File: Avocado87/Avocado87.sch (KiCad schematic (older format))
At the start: 185 parts, among them U1 proton_c

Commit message: Add footprint for proton-c
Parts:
- U1: footprint (none) -> proton_c:proton_c
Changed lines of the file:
@@
 F 0 "U1" H 9825 1027 50  0000 C CNN
 F 1 "proton_c" H 9825 936 50  0000 C CNN
-F 2 "" H 9700 2550 50  0001 C CNN
+F 2 "proton_c:proton_c" H 9700 2550 50  0001 C CNN
 F 3 "" H 9700 2550 50  0001 C CNN
 	1    9850 2550

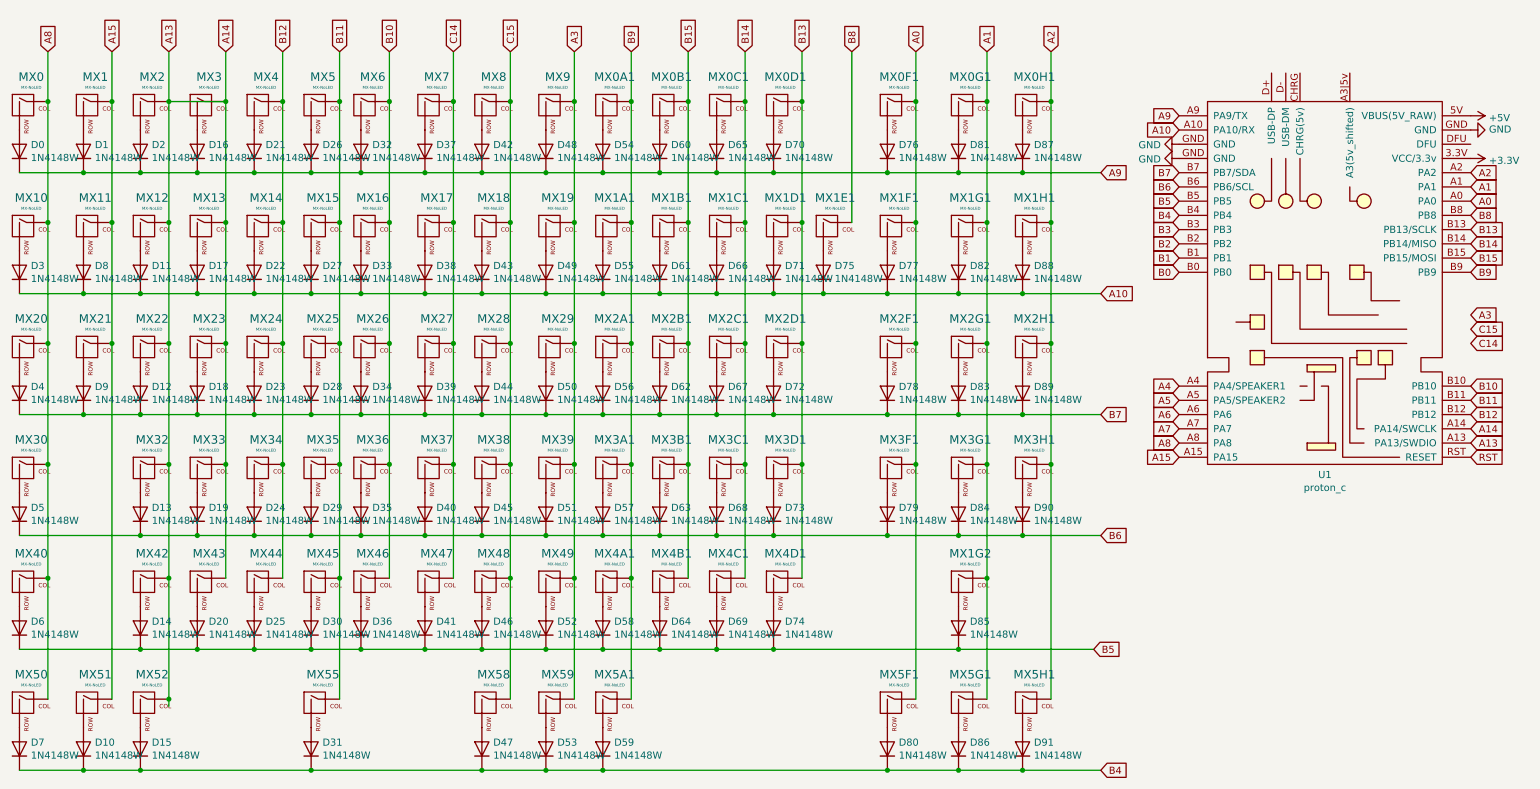
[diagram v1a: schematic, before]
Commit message: Footprint work
 - sort out issues with naming and missing switches
 - remove unused symbols from proton-c
 - start labeling diodes correctly
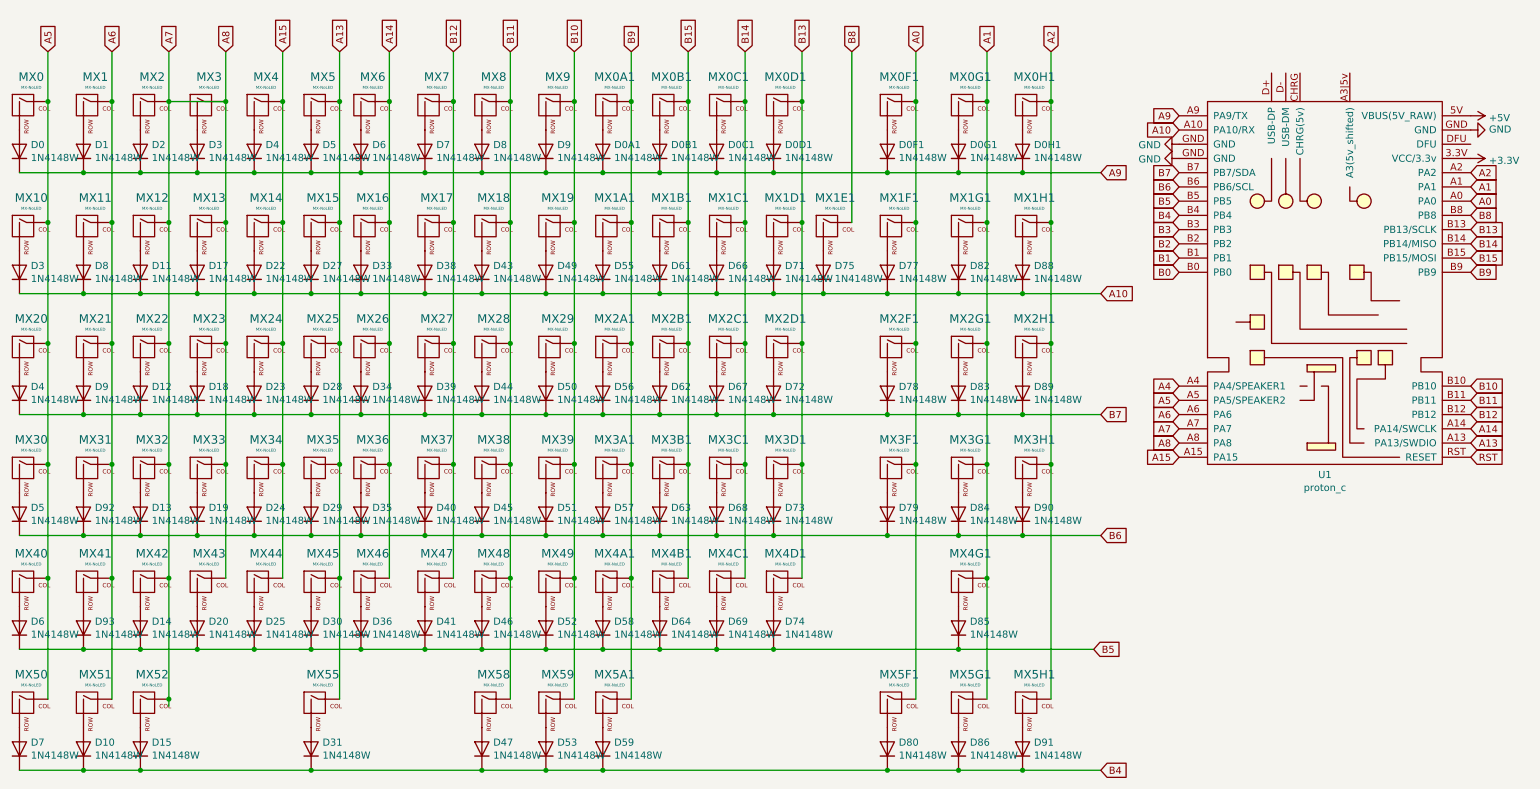
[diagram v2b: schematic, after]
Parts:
- added D92, D93: 1N4148W, Diodes_SMD:D_SOD-123, symbol Diode:1N4148W
- added MX31, MX41: MX-NoLED, MX_Only:MXOnly-1U-NoLED, symbol MX_Alps_Hybrid:MX-NoLED
- D0, D1, D10, D11, D12, D13, D14, D15, D17, D18, D19, D2, D20, D22, D23, D24, D25, D27, D28, D29, D3, D30, D31, D33, D34, D35, D36, D38, D39, D4, D40, D41, D43, D44, D45, D46, D47, D49, D5, D50, D51, D52, D53, D55, D56, D57, D58, D59, D6, D61, D62, D63, D64, D66, D67, D68, D69, D7, D71, D72, D73, D74, D75, D77, D78, D79, D8, D80, D82, D83, D84, D85, D86, D88, D89, D9, D90, D91: footprint Diode_SMD:D_SOD-123 -> Diodes_SMD:D_SOD-123
- D0A1: renamed from D54; footprint Diode_SMD:D_SOD-123 -> Diodes_SMD:D_SOD-123
- D0B1: renamed from D60; footprint Diode_SMD:D_SOD-123 -> Diodes_SMD:D_SOD-123
- D0C1: renamed from D65; footprint Diode_SMD:D_SOD-123 -> Diodes_SMD:D_SOD-123
- D0D1: renamed from D70; footprint Diode_SMD:D_SOD-123 -> Diodes_SMD:D_SOD-123
- D0F1: renamed from D76; footprint Diode_SMD:D_SOD-123 -> Diodes_SMD:D_SOD-123
- D0G1: renamed from D81; footprint Diode_SMD:D_SOD-123 -> Diodes_SMD:D_SOD-123
- D0H1: renamed from D87; footprint Diode_SMD:D_SOD-123 -> Diodes_SMD:D_SOD-123
- D3: renamed from D16; footprint Diode_SMD:D_SOD-123 -> Diodes_SMD:D_SOD-123
- D4: renamed from D21; footprint Diode_SMD:D_SOD-123 -> Diodes_SMD:D_SOD-123
- D5: renamed from D26; footprint Diode_SMD:D_SOD-123 -> Diodes_SMD:D_SOD-123
- D6: renamed from D32; footprint Diode_SMD:D_SOD-123 -> Diodes_SMD:D_SOD-123
- D7: renamed from D37; footprint Diode_SMD:D_SOD-123 -> Diodes_SMD:D_SOD-123
- D8: renamed from D42; footprint Diode_SMD:D_SOD-123 -> Diodes_SMD:D_SOD-123
- D9: renamed from D48; footprint Diode_SMD:D_SOD-123 -> Diodes_SMD:D_SOD-123
- renumbered MX1G2 to MX4G1
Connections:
- net A3 is gone; now on net B10: MX19.1 (COL), MX29.1 (COL), MX39.1 (COL), MX49.1 (COL), MX59.1 (COL), MX9.1 (COL)
- net C14 is gone; now on net B12: MX17.1 (COL), MX27.1 (COL), MX37.1 (COL), MX47.1 (COL), MX7.1 (COL)
- net C15 is gone; now on net B11: MX18.1 (COL), MX28.1 (COL), MX38.1 (COL), MX48.1 (COL), MX58.1 (COL), MX8.1 (COL)
- net A13: now also MX15.1 (COL), MX25.1 (COL), MX35.1 (COL), MX45.1 (COL), MX5.1 (COL), MX55.1 (COL); no longer MX12.1 (COL), MX13.1 (COL), MX2.1 (COL), MX22.1 (COL), MX23.1 (COL), MX3.1 (COL), MX32.1 (COL), MX33.1 (COL), MX42.1 (COL), MX43.1 (COL), MX52.1 (COL), U1.A14 (PA14/SWCLK)
- net A15: now also MX14.1 (COL), MX24.1 (COL), MX34.1 (COL), MX4.1 (COL), MX44.1 (COL); no longer MX1.1 (COL), MX11.1 (COL), MX21.1 (COL), MX51.1 (COL)
- net A5: now also MX0.1 (COL), MX10.1 (COL), MX20.1 (COL), MX30.1 (COL), MX40.1 (COL), MX50.1 (COL)
- net A6: now also MX1.1 (COL), MX11.1 (COL), MX21.1 (COL), MX51.1 (COL), MX31.1 (COL), MX41.1 (COL)
- net A7: now also MX12.1 (COL), MX13.1 (COL), MX2.1 (COL), MX22.1 (COL), MX23.1 (COL), MX3.1 (COL), MX32.1 (COL), MX33.1 (COL), MX42.1 (COL), MX43.1 (COL), MX52.1 (COL), U1.A8 (PA8)
- net B10: no longer MX16.1 (COL), MX26.1 (COL), MX36.1 (COL), MX46.1 (COL), MX6.1 (COL)
- net B11: no longer MX15.1 (COL), MX25.1 (COL), MX35.1 (COL), MX45.1 (COL), MX5.1 (COL), MX55.1 (COL)
- net B12: no longer MX14.1 (COL), MX24.1 (COL), MX34.1 (COL), MX4.1 (COL), MX44.1 (COL)
- net B5: now also D93.1 (K)
- net B6: now also D92.1 (K)
- removed net A8: MX0.1 (COL), MX10.1 (COL), MX20.1 (COL), MX30.1 (COL), MX40.1 (COL), MX50.1 (COL), U1.A8 (PA8)
- new net: D92.2 (A), MX31.2 (ROW)
- new net: D93.2 (A), MX41.2 (ROW)
- new net A14: MX16.1 (COL), MX26.1 (COL), MX36.1 (COL), MX46.1 (COL), MX6.1 (COL), U1.A14 (PA14/SWCLK)

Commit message: Placement and renames
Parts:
- removed D73, D74: 1N4148W, Diodes_SMD:D_SOD-123, symbol Diode:1N4148W
- removed MX3D1, MX4D1: MX-NoLED, MX_Only:MXOnly-1U-NoLED, symbol MX_Alps_Hybrid:MX-NoLED
- renumbered D3 to D10, D8 to D11, D11 to D12, D17 to D13, D22 to D14, D27 to D15, D33 to D16, D38 to D17, D43 to D18, D49 to D19, D55 to D1A1, D61 to D1B1, D66 to D1C1, D71 to D1D1, D75 to D1E1, D77 to D1F1, D82 to D1G1, D88 to D1H1, D4 to D20, D9 to D21, D12 to D22, D18 to D23, D23 to D24, D28 to D25, D34 to D26, D39 to D27, D44 to D28, D50 to D29, D56 to D2A1, D62 to D2B1, D67 to D2C1, D72 to D2D1, D78 to D2F1, D83 to D2G1, D89 to D2H1, D5 to D30, D92 to D31, D13 to D32, D19 to D33, D24 to D34, D29 to D35, D35 to D36, D40 to D37, D45 to D38, D51 to D39, D57 to D3A1, D63 to D3B1, D68 to D3C1, D79 to D3F1, D84 to D3G1, D90 to D3H1, D6 to D40, D93 to D41, D14 to D42, D20 to D43, D25 to D44, D30 to D45, D36 to D46, D41 to D47, D46 to D48, D52 to D49, D58 to D4A1, D64 to D4B1, D69 to D4C1, D85 to D4G1, D7 to D50, D10 to D51, D15 to D52, D31 to D53, D47 to D58, D53 to D59, D59 to D5A1, D80 to D5F1, D86 to D5G1, D91 to D5H1

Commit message: Routed PCB
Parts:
- renumbered D53 to D55
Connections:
- net A0: now also MX0C1.1 (COL), MX1C1.1 (COL), MX2C1.1 (COL), MX3C1.1 (COL), MX4C1.1 (COL); no longer MX0F1.1 (COL), MX1F1.1 (COL), MX2F1.1 (COL), MX3F1.1 (COL), MX5F1.1 (COL)
- net A1: now also MX0D1.1 (COL), MX1D1.1 (COL), MX2D1.1 (COL); no longer MX0G1.1 (COL), MX1G1.1 (COL), MX2G1.1 (COL), MX3G1.1 (COL), MX4G1.1 (COL), MX5G1.1 (COL)
- net A10: now also MX0F1.1 (COL), MX1F1.1 (COL), MX2F1.1 (COL), MX3F1.1 (COL), MX5F1.1 (COL); no longer D10.1 (K), D11.1 (K), D12.1 (K), D13.1 (K), D14.1 (K), D15.1 (K), D16.1 (K), D17.1 (K), D18.1 (K), D19.1 (K), D1A1.1 (K), D1B1.1 (K), D1C1.1 (K), D1D1.1 (K), D1E1.1 (K), D1F1.1 (K), D1G1.1 (K), D1H1.1 (K)
- net A13: now also MX17.1 (COL), MX27.1 (COL), MX37.1 (COL), MX47.1 (COL), MX7.1 (COL); no longer MX15.1 (COL), MX25.1 (COL), MX35.1 (COL), MX45.1 (COL), MX5.1 (COL), MX55.1 (COL)
- net A15: now also D30.1 (K), D31.1 (K), D32.1 (K), D33.1 (K), D34.1 (K), D35.1 (K), D36.1 (K), D37.1 (K), D38.1 (K), D39.1 (K), D3A1.1 (K), D3B1.1 (K), D3C1.1 (K), D3F1.1 (K), D3G1.1 (K), D3H1.1 (K); no longer MX14.1 (COL), MX24.1 (COL), MX34.1 (COL), MX4.1 (COL), MX44.1 (COL)
- net A2: now also D0.1 (K), D0A1.1 (K), D0B1.1 (K), D0C1.1 (K), D0D1.1 (K), D0F1.1 (K), D0G1.1 (K), D0H1.1 (K), D1.1 (K), D2.1 (K), D3.1 (K), D4.1 (K), D5.1 (K), D6.1 (K), D7.1 (K), D8.1 (K), D9.1 (K); no longer MX0H1.1 (COL), MX1H1.1 (COL), MX2H1.1 (COL), MX3H1.1 (COL), MX5H1.1 (COL)
- net A5: no longer MX0.1 (COL), MX10.1 (COL), MX20.1 (COL), MX30.1 (COL), MX40.1 (COL), MX50.1 (COL)
- net A6: no longer MX1.1 (COL), MX11.1 (COL), MX21.1 (COL), MX31.1 (COL), MX41.1 (COL), MX51.1 (COL)
- net A7: now also D50.1 (K), D51.1 (K), D52.1 (K), D55.1 (K), D58.1 (K), D59.1 (K), D5A1.1 (K), D5F1.1 (K), D5G1.1 (K), D5H1.1 (K); no longer MX12.1 (COL), MX13.1 (COL), MX2.1 (COL), MX22.1 (COL), MX23.1 (COL), MX3.1 (COL), MX32.1 (COL), MX33.1 (COL), MX42.1 (COL), MX43.1 (COL), MX52.1 (COL), U1.A8 (PA8)
- net A9: now also MX0G1.1 (COL), MX1G1.1 (COL), MX2G1.1 (COL), MX3G1.1 (COL), MX4G1.1 (COL), MX5G1.1 (COL); no longer D0.1 (K), D0A1.1 (K), D0B1.1 (K), D0C1.1 (K), D0D1.1 (K), D0F1.1 (K), D0G1.1 (K), D0H1.1 (K), D1.1 (K), D2.1 (K), D3.1 (K), D4.1 (K), D5.1 (K), D6.1 (K), D7.1 (K), D8.1 (K), D9.1 (K)
- net B1: now also MX0B1.1 (COL), MX1B1.1 (COL), MX2B1.1 (COL), MX3B1.1 (COL), MX4B1.1 (COL)
- net B10: now also MX13.1 (COL), MX23.1 (COL), MX3.1 (COL), MX33.1 (COL), MX43.1 (COL); no longer MX19.1 (COL), MX29.1 (COL), MX39.1 (COL), MX49.1 (COL), MX59.1 (COL), MX9.1 (COL)
- net B11: now also MX14.1 (COL), MX24.1 (COL), MX34.1 (COL), MX4.1 (COL), MX44.1 (COL); no longer MX18.1 (COL), MX28.1 (COL), MX38.1 (COL), MX48.1 (COL), MX58.1 (COL), MX8.1 (COL)
- net B12: now also MX15.1 (COL), MX25.1 (COL), MX35.1 (COL), MX45.1 (COL), MX5.1 (COL), MX55.1 (COL); no longer MX17.1 (COL), MX27.1 (COL), MX37.1 (COL), MX47.1 (COL), MX7.1 (COL)
- net B13: now also MX0.1 (COL), MX10.1 (COL), MX20.1 (COL), MX30.1 (COL), MX40.1 (COL), MX50.1 (COL); no longer MX0D1.1 (COL), MX1D1.1 (COL), MX2D1.1 (COL)
- net B14: now also MX1.1 (COL), MX11.1 (COL), MX21.1 (COL), MX31.1 (COL), MX41.1 (COL), MX51.1 (COL); no longer MX0C1.1 (COL), MX1C1.1 (COL), MX2C1.1 (COL), MX3C1.1 (COL), MX4C1.1 (COL)
- net B15: now also MX12.1 (COL), MX2.1 (COL), MX22.1 (COL), MX32.1 (COL), MX42.1 (COL), MX52.1 (COL); no longer MX0B1.1 (COL), MX1B1.1 (COL), MX2B1.1 (COL), MX3B1.1 (COL), MX4B1.1 (COL)
- net B2: now also MX0A1.1 (COL), MX1A1.1 (COL), MX2A1.1 (COL), MX3A1.1 (COL), MX4A1.1 (COL), MX5A1.1 (COL)
- net B3: now also MX19.1 (COL), MX29.1 (COL), MX39.1 (COL), MX49.1 (COL), MX59.1 (COL), MX9.1 (COL)
- net B4: now also MX18.1 (COL), MX28.1 (COL), MX38.1 (COL), MX48.1 (COL), MX58.1 (COL), MX8.1 (COL); no longer D50.1 (K), D51.1 (K), D52.1 (K), D55.1 (K), D58.1 (K), D59.1 (K), D5A1.1 (K), D5F1.1 (K), D5G1.1 (K), D5H1.1 (K)
- net B5: no longer D40.1 (K), D41.1 (K), D42.1 (K), D43.1 (K), D44.1 (K), D45.1 (K), D46.1 (K), D47.1 (K), D48.1 (K), D49.1 (K), D4A1.1 (K), D4B1.1 (K), D4C1.1 (K), D4G1.1 (K)
- net B6: now also D10.1 (K), D11.1 (K), D12.1 (K), D13.1 (K), D14.1 (K), D15.1 (K), D16.1 (K), D17.1 (K), D18.1 (K), D19.1 (K), D1A1.1 (K), D1B1.1 (K), D1C1.1 (K), D1D1.1 (K), D1E1.1 (K), D1F1.1 (K), D1G1.1 (K), D1H1.1 (K); no longer D30.1 (K), D31.1 (K), D32.1 (K), D33.1 (K), D34.1 (K), D35.1 (K), D36.1 (K), D37.1 (K), D38.1 (K), D39.1 (K), D3A1.1 (K), D3B1.1 (K), D3C1.1 (K), D3F1.1 (K), D3G1.1 (K), D3H1.1 (K)
- net B7: now also MX0H1.1 (COL), MX1H1.1 (COL), MX2H1.1 (COL), MX3H1.1 (COL), MX5H1.1 (COL); no longer D20.1 (K), D21.1 (K), D22.1 (K), D23.1 (K), D24.1 (K), D25.1 (K), D26.1 (K), D27.1 (K), D28.1 (K), D29.1 (K), D2A1.1 (K), D2B1.1 (K), D2C1.1 (K), D2D1.1 (K), D2F1.1 (K), D2G1.1 (K), D2H1.1 (K)
- net B9: now also D20.1 (K), D21.1 (K), D22.1 (K), D23.1 (K), D24.1 (K), D25.1 (K), D26.1 (K), D27.1 (K), D28.1 (K), D29.1 (K), D2A1.1 (K), D2B1.1 (K), D2C1.1 (K), D2D1.1 (K), D2F1.1 (K), D2G1.1 (K), D2H1.1 (K); no longer MX0A1.1 (COL), MX1A1.1 (COL), MX2A1.1 (COL), MX3A1.1 (COL), MX4A1.1 (COL), MX5A1.1 (COL)
- new net A8: D40.1 (K), D41.1 (K), D42.1 (K), D43.1 (K), D44.1 (K), D45.1 (K), D46.1 (K), D47.1 (K), D48.1 (K), D49.1 (K), D4A1.1 (K), D4B1.1 (K), D4C1.1 (K), D4G1.1 (K), U1.A8 (PA8)
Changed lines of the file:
@@
 $EndComp
 $Comp
-L Diode:1N4148W D53
+L Diode:1N4148W D55
 U 1 1 5DA675DF
 P 2700 6000
-F 0 "D53" V 2746 5920 50  0000 R CNN
+F 0 "D55" V 2746 5920 50  0000 R CNN
 F 1 "1N4148W" V 2655 5920 50  0000 R CNN
 F 2 "Diodes_SMD:D_SOD-123" H 2700 5825 50  0001 C CNN
@@
 	1700 4000 1700 4800
 Connection ~ 1700 4000
-Wire Wire Line
-	1700 1450 2100 1450
 Connection ~ 1700 4800
 Wire Wire Line
@@
 Wire Wire Line
 	7700 6150 7250 6150
-Text GLabel 8250 1950 2    50   Input ~ 0
+Text GLabel 7450 1100 1    50   Input ~ 0
 A9
+Text GLabel 7900 1100 1    50   Input ~ 0
+B7
+Text GLabel 6950 1100 1    50   Input ~ 0
+A10
+Text GLabel 8250 2800 2    50   Input ~ 0
+B6
 Text GLabel 8250 3650 2    50   Input ~ 0
-B7
-Text GLabel 8250 2800 2    50   Input ~ 0
-A10
-Text GLabel 8250 4500 2    50   Input ~ 0
-B6
-Text GLabel 8200 5300 2    50   Input ~ 0
-B5
-Text GLabel 8250 6150 2    50   Input ~ 0
-B4
+B9
 Connection ~ 1300 1450
 Wire Wire Line
@@
 Wire Wire Line
 	850  1450 850  1100
-Text GLabel 7900 1100 1    50   Input ~ 0
+Text GLabel 8250 1950 2    50   Input ~ 0
 A2
-Text GLabel 7450 1100 1    50   Input ~ 0
+Text GLabel 6150 1100 1    50   Input ~ 0
 A1
-Text GLabel 6950 1100 1    50   Input ~ 0
+Text GLabel 5750 1100 1    50   Input ~ 0
 A0
 Text GLabel 6500 1100 1    50   Input ~ 0
 B8
-Text GLabel 6150 1100 1    50   Input ~ 0
+Text GLabel 850  1100 1    50   Input ~ 0
 B13
-Text GLabel 5750 1100 1    50   Input ~ 0
+Text GLabel 1300 1100 1    50   Input ~ 0
 B14
-Text GLabel 5350 1100 1    50   Input ~ 0
+Text GLabel 1700 1100 1    50   Input ~ 0
 B15
-Text GLabel 4950 1100 1    50   Input ~ 0
-B9
-Text GLabel 4550 1100 1    50   Input ~ 0
+Text GLabel 8250 4500 2    50   Input ~ 0
+A15
+Text GLabel 2100 1100 1    50   Input ~ 0
 B10
-Text GLabel 4100 1100 1    50   Input ~ 0
+Text GLabel 2500 1100 1    50   Input ~ 0
 B11
-Text GLabel 3700 1100 1    50   Input ~ 0
+Text GLabel 2900 1100 1    50   Input ~ 0
 B12
 Text GLabel 3250 1100 1    50   Input ~ 0
 A14
-Text GLabel 2900 1100 1    50   Input ~ 0
+Text GLabel 3700 1100 1    50   Input ~ 0
 A13
-Text GLabel 2500 1100 1    50   Input ~ 0
-A15
-Text GLabel 2100 1100 1    50   Input ~ 0
+Text GLabel 8200 5300 2    50   Input ~ 0
 A8
-Text GLabel 1700 1100 1    50   Input ~ 0
-A7
-Text GLabel 1300 1100 1    50   Input ~ 0
-A6
-Text GLabel 850  1100 1    50   Input ~ 0
-A5
+Text GLabel 5350 1100 1    50   Input ~ 0
+B1
+Text GLabel 4950 1100 1    50   Input ~ 0
+B2
 $Comp
 L power:+3.3V #PWR0101
@@
 Connection ~ 7250 5300
 Connection ~ 5550 5300
+Text GLabel 4550 1100 1    50   Input ~ 0
+B3
+Text GLabel 4100 1100 1    50   Input ~ 0
+B4
+Text GLabel 8250 6150 2    50   Input ~ 0
+A7
 $EndSCHEMATC

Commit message: Fine tuning
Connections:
- net A0: now also MX0D1.1 (COL), MX1D1.1 (COL), MX2D1.1 (COL); no longer MX0C1.1 (COL), MX1C1.1 (COL), MX2C1.1 (COL), MX3C1.1 (COL), MX4C1.1 (COL)
- net A1: now also MX0C1.1 (COL), MX1C1.1 (COL), MX2C1.1 (COL), MX3C1.1 (COL), MX4C1.1 (COL); no longer MX0D1.1 (COL), MX1D1.1 (COL), MX2D1.1 (COL)
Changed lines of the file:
@@
 Text GLabel 8250 1950 2    50   Input ~ 0
 A2
+Text GLabel 5750 1100 1    50   Input ~ 0
+A1
 Text GLabel 6150 1100 1    50   Input ~ 0
-A1
-Text GLabel 5750 1100 1    50   Input ~ 0
 A0
 Text GLabel 6500 1100 1    50   Input ~ 0

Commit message: Add i2c and underglow to pcb
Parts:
- added J1: Conn_01x04_Female, Connectors:Fan_Pin_Header_Straight_1x04, symbol Connector:Conn_01x04_Female
- added J2: Conn_01x03_Female, Connectors:PINHEAD1-3, symbol Connector:Conn_01x03_Female
- D0, D0A1, D0B1, D0C1, D0D1, D0F1, D0G1, D0H1, D1, D10, D11, D12, D13, D14, D15, D16, D17, D18, D19, D1A1, D1B1, D1C1, D1D1, D1E1, D1F1, D1G1, D1H1, D2, D20, D21, D22, D23, D24, D25, D26, D27, D28, D29, D2A1, D2B1, D2C1, D2D1, D2F1, D2G1, D2H1, D3, D30, D31, D32, D33, D34, D35, D36, D37, D38, D39, D3A1, D3B1, D3C1, D3F1, D3G1, D3H1, D4, D40, D41, D42, D43, D44, D45, D46, D47, D48, D49, D4A1, D4B1, D4C1, D4G1, D5, D50, D51, D52, D55, D58, D59, D5A1, D5F1, D5G1, D5H1, D6, D7, D8, D9: footprint Diodes_SMD:D_SOD-123 -> random-keyboard-parts:D_SOD-123-Pretty
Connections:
- net +3V3: now also J1.1 (Pin_1)
- net +5V: now also J2.1 (Pin_1)
- net B0: now also MX0H1.1 (COL), MX1H1.1 (COL), MX2H1.1 (COL), MX3H1.1 (COL), MX5H1.1 (COL)
- net B5: now also D10.1 (K), D11.1 (K), D12.1 (K), D13.1 (K), D14.1 (K), D15.1 (K), D16.1 (K), D17.1 (K), D18.1 (K), D19.1 (K), D1A1.1 (K), D1B1.1 (K), D1C1.1 (K), D1D1.1 (K), D1E1.1 (K), D1F1.1 (K), D1G1.1 (K), D1H1.1 (K)
- net B6: now also J1.2 (Pin_2); no longer D10.1 (K), D11.1 (K), D12.1 (K), D13.1 (K), D14.1 (K), D15.1 (K), D16.1 (K), D17.1 (K), D18.1 (K), D19.1 (K), D1A1.1 (K), D1B1.1 (K), D1C1.1 (K), D1D1.1 (K), D1E1.1 (K), D1F1.1 (K), D1G1.1 (K), D1H1.1 (K)
- net B7: now also J1.3 (Pin_3); no longer MX0H1.1 (COL), MX1H1.1 (COL), MX2H1.1 (COL), MX3H1.1 (COL), MX5H1.1 (COL)
- net GND: now also J1.4 (Pin_4), J2.3 (Pin_3)
- net A3: now reaches U1.A3|5v (A3(5v_shifted))
- net A3: now also J2.2 (Pin_2)
